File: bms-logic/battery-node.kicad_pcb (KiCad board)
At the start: 2 copper layers, 270.1 x 230.8 mm, 222 parts, among them J5 Connector, USB-TYPE-C-16P, Q1 PBSS4350T,215, Q10 PBSS4350T,215, Q11 PBSS4350T,215, Q12 PBSS4350T,215, Q13 PBSS4350T,215, Q14 PBSS4350T,215, Q15 PBSS4350T,215, Q16 PBSS4350T,215, Q17 PBSS4350T,215, Q18 PBSS4350T,215, Q19 PBSS4350T,215, Q2 BSS123, Q3 DMZ6012E, Q4 DMZ6012E, Q5 PBSS4350T,215, Q6 PBSS4350T,215, Q7 PBSS4350T,215, Q8 PBSS4350T,215, Q9 PBSS4350T,215, U1 ESP32-H2-MINI-1-H2S, U10 TCAN334D, U2 BQ76972PFBR, U3 2SC2383_C41375137, U4 XC6206P332MR, U5 MP9485GN-Z, U6 MIE1W0505BGLVH-3R-Z, U7 ISO7041FDBQ, U8 ADUM3160, U9 LTV-217-B-G

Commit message: started afe layout
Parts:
- removed the C21 at (34.3, 53.0)
- removed the C3 at (85.4, 25.2)
- removed the C4 at (85.4, 27.1)
- removed the C5 at (85.4, 28.9)
- removed the C50 at (110.6, -16.8)
- removed the C51 at (97.0, -16.8)
- removed the C52 at (102.2, -28.7)
- removed the C53 at (83.4, -5.49)
- removed the C6 at (85.4, 30.8)
- removed D6: SMCJ64CA, PCM_JLCPCB:D_SMC
- added C17: 220nF, PCM_JLCPCB:C_0805, B.Cu at (63.5, 25.7)
- added C36: 220nF, PCM_JLCPCB:C_0805, B.Cu at (63.5, 29.7)
- added C37: 220nF, PCM_JLCPCB:C_0805, B.Cu at (63.5, 33.6)
- added C38: 220nF, PCM_JLCPCB:C_0805, B.Cu at (63.5, 37.6)
- added C39: 220nF, PCM_JLCPCB:C_0805, B.Cu at (63.5, 41.6)
- added D16: BZT52C75, PCM_JLCPCB:D_SOD-123, F.Cu at (59.4, -99.3)
- added D17: BZT52C75, PCM_JLCPCB:D_SOD-123, F.Cu at (59.4, -95.9)
- C1, C2, C40, C41, C42, C43, C44, C45, C46, C47, C48, C49, Q1, Q10, Q11, Q12, Q13, Q14, Q15, Q16, Q17, Q18, Q19, Q6, Q7, Q8, Q9, R13, R14, R49, R50, R52, R53, R55, R56, R58, R59, R61, R62, R64, R65, R67, R68, R70, R71, R73, R74, R76, R77, R79, R80, R82, R83, R85, R86, R88, R89: moved to B.Cu
- CN1, CN2, CN3, CN4: value ~ -> A2001WR-S-2P
- D14: value ~ -> BAT20JFILM
- LED1: value ~ -> MHT136UBCT
- U2: renamed from U11; value ~ -> A2001WR-S-12PD01
- U3: renamed from U12; value ~ -> A2001WR-S-08PD01
- U4: renamed from U2; moved to B.Cu
- moved CN4 297.9 mm to (354.8, -26.8)
- moved CN3 294.0 mm to (343.9, -26.8)
- moved C50 280.1 mm to (318.2, -20.4)
- moved CN1 280.1 mm to (322.2, -26.8)
- moved C52 272.5 mm to (318.2, -16.7)
- moved CN2 272.1 mm to (333.1, -26.8)
- moved C53 266.1 mm to (318.2, -14.8)
- moved C51 261.4 mm to (318.2, -18.5)
- moved REF** 260.6 mm to (69.8, -10.2)
- moved JP3 178.3 mm to (219.2, -74.2)
- moved JP4 178.3 mm to (219.2, -70.6)
- moved Q4 175.8 mm to (214.3, -68.8)
- moved Q3 175.8 mm to (214.3, -73.5)
- moved D10 170.9 mm to (208.8, -64.2)
- moved D7 170.9 mm to (208.8, -74.3)
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- renumbered C14 to C10, C15 to C11, C16 to C12, C17 to C13, C18 to C14, C19 to C15, C20 to C16, C22 to C18, C23 to C19, C24 to C20, C25 to C21, C26 to C22, C27 to C23, C28 to C24, C29 to C25, C30 to C26, C31 to C27, C32 to C28, C33 to C29, C7 to C3, C34 to C30, C35 to C31, C36 to C32, C37 to C33, C38 to C34, C39 to C35, C8 to C4, C9 to C5, C6 to C50, C54 to C51, C55 to C52, C56 to C53, C10 to C6, C11 to C7, C12 to C8, C13 to C9, J5 to J3, U8 to U10, U9 to U11, U10 to U12, U3 to U5, U4 to U6, U5 to U7, U6 to U8, U7 to U9
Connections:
- C40 pad 1: /AFE/VC3 -> /AFE/VC7
- C40 pad 2: /AFE/VC2 -> /AFE/VC6
- C41 pad 1: /AFE/VC4 -> /AFE/VC8
- C41 pad 2: /AFE/VC3 -> /AFE/VC7
- C42 pad 1: /AFE/VC5 -> /AFE/VC9
- C42 pad 2: /AFE/VC4 -> /AFE/VC8
- C43 pad 1: /AFE/VC6 -> /AFE/VC10
- C43 pad 2: /AFE/VC5 -> /AFE/VC9
- C44 pad 1: /AFE/VC7 -> /AFE/VC11
- C44 pad 2: /AFE/VC6 -> /AFE/VC10
- C45 pad 1: /AFE/VC8 -> /AFE/VC12
- C45 pad 2: /AFE/VC7 -> /AFE/VC11
- C46 pad 1: /AFE/VC9 -> /AFE/VC13
- C46 pad 2: /AFE/VC8 -> /AFE/VC12
- C47 pad 1: /AFE/VC10 -> /AFE/VC14
- C47 pad 2: /AFE/VC9 -> /AFE/VC13
- C48 pad 1: /AFE/VC11 -> /AFE/VC15
- C48 pad 2: /AFE/VC10 -> /AFE/VC14
- C49 pad 1: /AFE/VC12 -> /AFE/VC16
- C49 pad 2: /AFE/VC11 -> /AFE/VC15
- R1 pad 2: +3V3 -> 3V3
- R2 pad 2: +3V3 -> 3V3
- R4 pad 2: +3V3 -> 3V3
- TP10 pad 1: +3V3 -> 3V3
- U1 pad 3: +3V3 -> 3V3
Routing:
- net Net-(Q7-C): track 0.00 -> 3.83 mm, vias 0 -> 1
- net Net-(Q19-C): track 0.00 -> 3.83 mm, vias 0 -> 1
- net Net-(Q18-C): track 0.00 -> 3.83 mm, vias 0 -> 1
- net Net-(Q17-C): track 0.00 -> 3.83 mm, vias 0 -> 1
- net Net-(Q16-C): track 0.00 -> 3.83 mm, vias 0 -> 1
- net Net-(Q15-C): track 0.00 -> 3.83 mm, vias 0 -> 1
- net Net-(Q14-C): track 0.00 -> 3.83 mm, vias 0 -> 1
- net Net-(Q13-C): track 0.00 -> 3.83 mm, vias 0 -> 1
- net Net-(Q12-C): track 0.00 -> 3.83 mm, vias 0 -> 1
- net Net-(Q6-C): track 0.00 -> 3.83 mm, vias 0 -> 1
- net Net-(Q5-C): track 0.00 -> 3.83 mm, vias 0 -> 1
- net Net-(Q1-C): track 0.00 -> 3.83 mm, vias 0 -> 1
- net Net-(Q9-C): track 0.00 -> 3.83 mm, vias 0 -> 1
- net Net-(Q8-C): track 0.00 -> 3.83 mm, vias 0 -> 1
- net Net-(Q11-C): track 0.00 -> 3.83 mm, vias 0 -> 1
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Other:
- copper layers 2 -> 4

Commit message: power supply layout
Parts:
- added TP23: IO25, TestPoint:TestPoint_Pad_D1.0mm, F.Cu at (216.9, 43.9)
- C18, C20, C22, C24, C32, C33, C34, C35, D13, D2, R12, R34, R35, U10: moved to B.Cu
- moved C20 193.5 mm to (76.7, 46.7), turned to 0 degrees
- moved C24 192.8 mm to (76.7, 56.4)
- moved U7 184.7 mm to (76.4, 49.5), turned to -90 degrees
- moved C19 182.3 mm to (76.7, 44.4), turned to 0 degrees
- moved L1 181.2 mm to (76.9, 55.9), turned to -90 degrees
- moved D13 177.8 mm to (74.9, 50.3)
- moved TP15 177.6 mm to (76.7, 59.2)
- moved R33 171.9 mm to (77.8, 35.2)
- moved R35 168.6 mm to (78.2, 48.2), turned to 180 degrees
- moved C18 167.7 mm to (76.7, 44.4), turned to 0 degrees
- moved R34 165.9 mm to (78.7, 49.8)
- moved JP5 165.1 mm to (75.8, 35.1)
- moved C23 164.7 mm to (74.1, 57.1)
- moved C21 162.6 mm to (74.1, 54.3), turned to -90 degrees
- moved C22 162.2 mm to (78.0, 51.3), turned to 0 degrees
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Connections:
- net /ISOLATED_COMMS/CAN_SHUTDOWN renamed /CAN_SHUTDOWN
- net /ISOLATED_COMMS/CAN_SLEEP renamed /CAN_SLEEP
- net /ISOLATED_COMMS/EN_ISO_PWR renamed /EN_ISO_PWR
- net /ISOLATED_COMMS/USB_N renamed /USB_D-
- net /ISOLATED_COMMS/USB_P renamed /USB_D+
- net /ISOLATED_COMMS/USB_nINT renamed /USB_nINT
- C22 pad 1: GND -> Net-(U7-FB)
- R34 pad 2: GND -> Net-(U7-FB)
- R35 pad 1: GND -> Net-(U7-FB)
- U1 pad 24: unconnected-(U1-IO22-Pad24) -> Net-(U1-IO22)
- U7 pad 1: GND -> Net-(U7-FB)
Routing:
- net (no net): track 0.00 -> 34.7 mm
- net GND: track 2.30 -> 18.9 mm, vias 2 -> 8
- net 5V0_SW: track 0.00 -> 12.8 mm, vias 0 -> 6
- net Net-(U7-BST): track 0.00 -> 10.4 mm, vias 0 -> 2
- net TOP_CELL: track 0.00 -> 8.87 mm, vias 0 -> 2
- net Net-(U7-FB): track 0.00 -> 5.54 mm, vias 0 -> 1
- net /AFE/VC0: track 0.00 -> 5.08 mm, vias 0 -> 1
- net Net-(D14-A): track 0.00 -> 4.23 mm
- net Net-(Q19-B): track 0.00 -> 4.17 mm
- net /EN_ISO_PWR: track 0.00 -> 4.14 mm
- net /AFE/Cell16: track 0.00 -> 3.58 mm, vias 0 -> 1
- net /AFE/VC16: track 0.00 -> 2.04 mm
- net Net-(U7-SW): track 0.00 -> 2.01 mm, vias 0 -> 1
- net GNDISO: track 0.00 -> 1.99 mm, vias 0 -> 2
- net 3V3: track 0.00 -> 1.68 mm, vias 0 -> 1
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- added copper zone on B.Cu, net /AFE/VC15
- added copper zone on In2.Cu, net 3V3
- added copper zone on B.Cu, net 5V0_ISO_SW
- added copper zone on B.Cu, net 5V0_SW
- added copper zone on F.Cu, net 5V0_SW
- added copper zone on B.Cu, net GND
- added copper zone on F.Cu, net GND
- added copper zone on In1.Cu, net GND
- added copper zone on F.Cu, net Net-(U7-SW)
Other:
- board size 270.1 x 230.8 mm -> 40.1 x 65.3 mm

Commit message: isolated comms
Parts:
- removed C50, C51, C52, C53: 470pF, PCM_JLCPCB:C_0402
- removed CN2, CN3, CN4: A2001WR-S-2P, JLCImport:A2001WR-S-2P
- removed JP6: SolderJumper_2_Open, Jumper:SolderJumper-2_P1.3mm_Open_RoundedPad1.0x1.5mm
- removed REF**: Untitled, ct_lib:Untitled
- removed TP1, TP10, TP11, TP2, TP23, TP3, TP4, TP5, TP6: IO25, TestPoint:TestPoint_Pad_D1.0mm
- removed TP16, TP17, TP18, TP19: IO8, TestPoint:TestPoint_Pad_D1.0mm
- removed TP7, TP8, TP9: IO9, TestPoint:TestPoint_Pad_D1.0mm
- removed U3: A2001WR-S-08PD01, JLCImport:A2001WR-S-08PD01
- added C54: 100nF, PCM_JLCPCB:C_0402, F.Cu at (79.3, 61.1)
- added C55: 100nF, PCM_JLCPCB:C_0402, F.Cu at (77.0, 72.9)
- added CN5: S4B-ZR-SM4A-TF_LF_SN, Connector_JST:JST_ZH_S4B-ZR-SM4A-TF_1x04-1MP_P1.50mm_Horizontal, F.Cu at (68.1, 79.5)
- C13, C27, C28, C30, C31, D11, R38, R39, R42, R43, R44, U11, U12: moved to B.Cu
- CN1: value A2001WR-S-2P -> S12B-ZR-SM4A-TF; footprint JLCImport:A2001WR-S-2P -> Connector_JST:JST_ZH_S12B-ZR-SM4A-TF_1x12-1MP_P1.50mm_Horizontal
- U2: value A2001WR-S-12PD01 -> S8B-ZR-SM4A-TF_LF_SN; footprint JLCImport:A2001WR-S-12PD01 -> Connector_JST:JST_ZH_S8B-ZR-SM4A-TF_1x08-1MP_P1.50mm_Horizontal
- U4: moved to F.Cu
- moved CN1 294.1 mm to (45.3, 72.3), turned to -90 degrees
- moved R1 135.3 mm to (116.5, 40.6)
- moved R2 135.3 mm to (118.3, 40.6)
- moved R4 123.6 mm to (119.1, 42.9)
- moved LED1 121.6 mm to (116.6, 43.7)
- moved R3 116.4 mm to (120.2, 40.6)
- moved C28 112.0 mm to (68.1, 61.0), turned to -90 degrees
- moved R40 109.8 mm to (68.0, 71.3), turned to -90 degrees
- moved R38 109.6 mm to (72.1, 59.4), turned to 0 degrees
- moved C27 109.6 mm to (70.1, 59.4), turned to 180 degrees
- moved R39 109.4 mm to (74.2, 59.4), turned to 180 degrees
- moved U11 109.0 mm to (81.3, 67.3)
- moved R42 107.0 mm to (74.0, 72.7), turned to 180 degrees
- moved U12 106.7 mm to (71.1, 79.0), turned to -90 degrees
- moved C30 106.3 mm to (69.3, 73.2), turned to -90 degrees
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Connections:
- C31 pad 1: GND -> GNDISO
- CN1 pad 2: /AFE/TEMP_CELLS_1 -> /AFE/Cell0
- CN1 pad 3: GND -> /AFE/Cell2
- CN1 pad 4: GND -> /AFE/Cell4
- U2 pad 1: unconnected-(U2-Pad1) -> /AFE/Cell1
- U2 pad 2: /AFE/Cell0 -> /AFE/Cell3
- U2 pad 3: /AFE/Cell2 -> /AFE/Cell5
- U2 pad 4: /AFE/Cell4 -> /AFE/Cell7
- U2 pad 5: /AFE/Cell6 -> /AFE/Cell9
- U2 pad 6: /AFE/Cell8 -> /AFE/Cell11
- U2 pad 7: /AFE/Cell10 -> /AFE/Cell13
- U2 pad 8: /AFE/Cell12 -> /AFE/Cell15
- U9 pad 13: Net-(JP6-A) -> unconnected-(U9-OUTB-Pad13)
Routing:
- net GNDISO: track 1.99 -> 68.5 mm, vias 2 -> 15
- net (no net): track 34.7 -> 0.00 mm
- net Net-(U12-CANH): track 0.00 -> 18.9 mm, vias 0 -> 1
- net Net-(U12-STB): track 0.00 -> 17.5 mm, vias 0 -> 3
- net Net-(JP7-A): track 0.00 -> 15.3 mm, vias 0 -> 1
- net Net-(U12-TXD): track 0.00 -> 13.8 mm, vias 0 -> 1
- net /ISOLATED_COMMS/USB_ISO_N: track 0.00 -> 10.2 mm, vias 0 -> 1
- net VBUS_ISO: track 0.00 -> 9.80 mm, vias 0 -> 4
- net Net-(U12-RXD): track 0.00 -> 9.65 mm, vias 0 -> 1
- net /ISOLATED_COMMS/USB_ISO_P: track 0.00 -> 8.61 mm, vias 0 -> 1
- net Net-(U10-SPD): track 0.00 -> 7.04 mm, vias 0 -> 1
- net 5V0_ISO_SW: track 0.00 -> 6.77 mm, vias 3 -> 6
- net GND: track 18.9 -> 23.8 mm, vias 8 -> 18
- net Net-(D11-K): track 0.00 -> 3.80 mm, vias 0 -> 1
- net Net-(U10-VDD2): track 0.00 -> 3.30 mm
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- added copper zone on F.Cu, net 3V3
- added copper zone on F.Cu, net 5V0_ISO_SW
- added copper zone on In2.Cu, net 5V0_ISO_SW
- added copper zone on In2.Cu, net 5V0_SW
- added copper zone on B.Cu, net GNDISO
- added copper zone on F.Cu, net GNDISO
- added copper zone on In1.Cu, net GNDISO
- added copper zone on In2.Cu, net VBUS_ISO
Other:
- board size 40.1 x 65.3 mm -> 45.2 x 65.3 mm
- board text added: "Add mounting holes for a custom heatsink over resistors? or just glue aluminum to them Or do nothing! They're rated for it anyways"
- board text added: "COMMS connection here?"
- board text added: "Cell connectors here"
- board text added: "Make mezzanine connector on bottom side 1.27 pitch ribbon on top side best of both worlds"

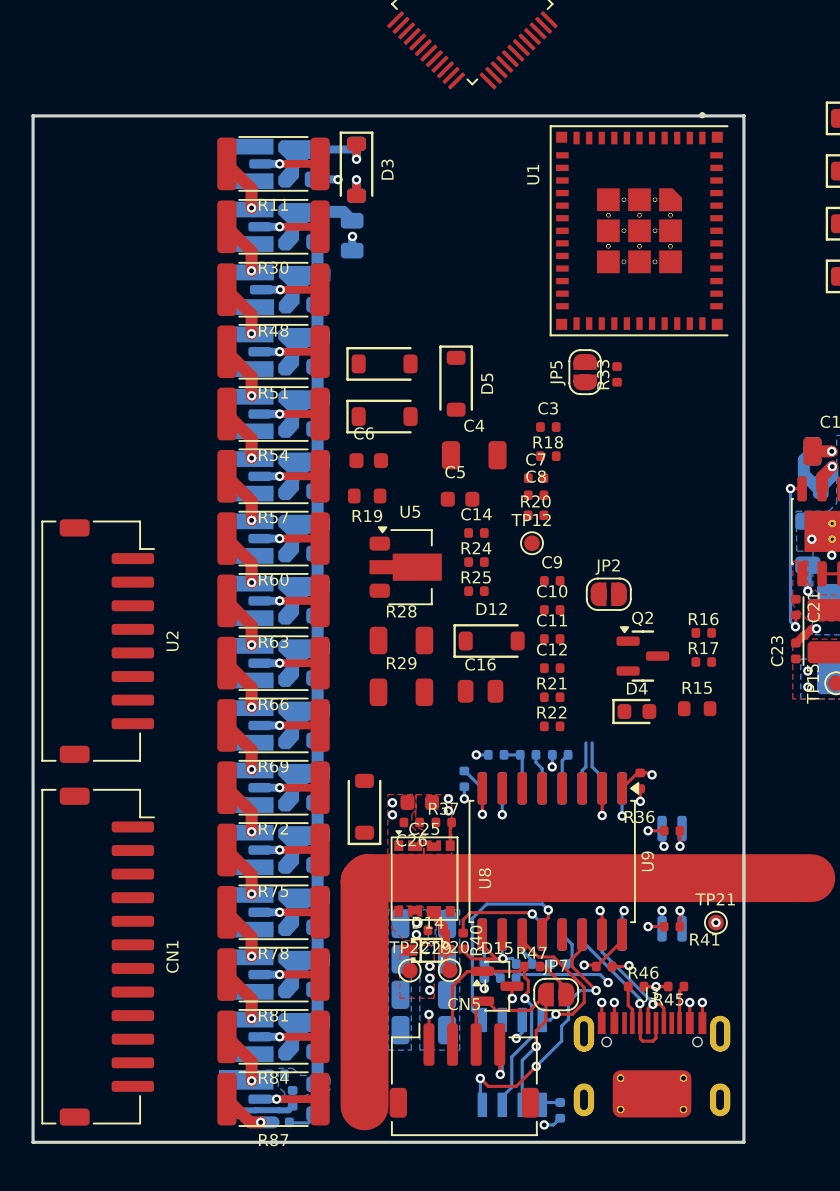
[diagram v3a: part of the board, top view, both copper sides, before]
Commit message: trying to flip resistor directions (fail)
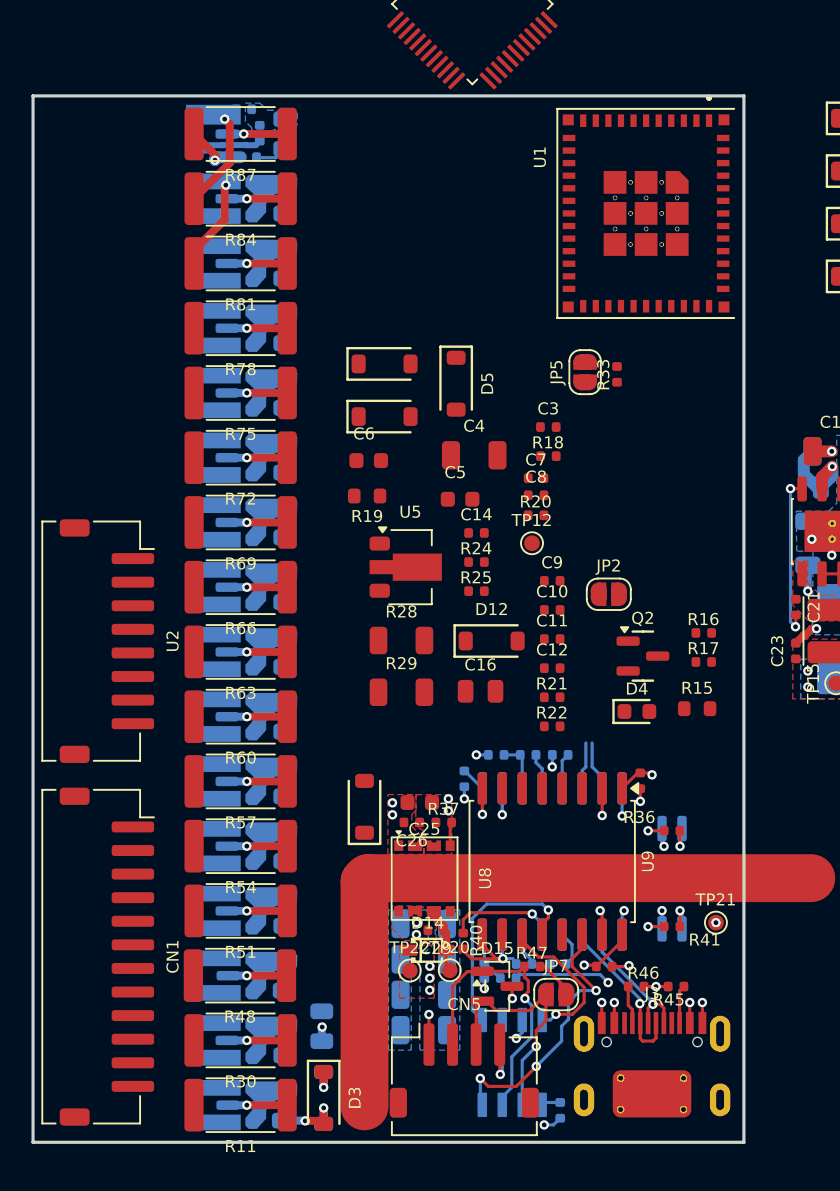
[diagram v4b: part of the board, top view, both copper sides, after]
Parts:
- moved R12 61.4 mm to (54.4, 21.4)
- moved C49 61.4 mm to (56.6, 19.9)
- moved Q19 61.4 mm to (52.0, 19.9)
- moved R87 61.4 mm to (53.8, 19.9)
- moved R88 61.4 mm to (55.1, 19.9)
- moved R89 61.4 mm to (54.0, 18.4)
- moved C2 59.9 mm to (56.6, 81.7)
- moved Q1 59.9 mm to (52.1, 81.7)
- moved R11 59.9 mm to (53.8, 81.7)
- moved R13 59.9 mm to (54.0, 82.9)
- moved R14 59.9 mm to (54.0, 80.6)
- moved D2 59.1 mm to (59.1, 81.3)
- moved D3 59.1 mm to (59.1, 81.3)
- moved C48 53.3 mm to (56.6, 24.1)
- moved Q18 53.3 mm to (52.0, 24.1)
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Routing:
- net /AFE/Cell8: track 3.45 -> 0.00 mm, vias 1 -> 0
- net /AFE/Cell7: track 3.45 -> 0.00 mm, vias 1 -> 0
- net /AFE/Cell6: track 3.45 -> 0.00 mm, vias 1 -> 0
- net /AFE/Cell5: track 3.45 -> 0.00 mm, vias 1 -> 0
- net /AFE/Cell4: track 3.45 -> 0.00 mm, vias 1 -> 0
- net /AFE/Cell13: track 3.45 -> 0.00 mm, vias 1 -> 0
- net /AFE/Cell12: track 3.45 -> 0.00 mm, vias 1 -> 0
- net /AFE/Cell9: track 3.45 -> 0.00 mm, vias 1 -> 0
- net /AFE/Cell11: track 3.45 -> 0.00 mm, vias 1 -> 0
- net /AFE/Cell10: track 3.45 -> 0.00 mm, vias 1 -> 0
- net /AFE/Cell3: track 3.45 -> 0.00 mm, vias 1 -> 0
- net /AFE/Cell2: track 3.45 -> 0.00 mm, vias 1 -> 0
- net /AFE/Cell1: track 3.45 -> 0.00 mm, vias 1 -> 0
- net /AFE/VC0: track 5.08 -> 1.96 mm
- net /AFE/Cell15: track 3.45 -> 6.14 mm
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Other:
- board size 45.2 x 65.3 mm -> 45.2 x 66.5 mm
- board text removed: "Cell connectors here"

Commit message: diagonal
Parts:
- added C50: 470pF, PCM_JLCPCB:C_0402, F.Cu at (34.8, 30.0)
- added C51: 470pF, PCM_JLCPCB:C_0402, F.Cu at (37.0, 30.0)
- added C56: 470pF, PCM_JLCPCB:C_0402, F.Cu at (34.8, 31.9)
- added C57: 470pF, PCM_JLCPCB:C_0402, F.Cu at (37.0, 31.9)
- added CN2: S4B-ZR-SM4A-TF_LF_SN, JLCImport:JST_ZH_S4B-ZR-SM4A-TF_1x04-1MP_P1.50mm_Horizontal, F.Cu at (45.3, 25.2)
- added CN3: S4B-ZR-SM4A-TF_LF_SN, JLCImport:JST_ZH_S4B-ZR-SM4A-TF_1x04-1MP_P1.50mm_Horizontal, F.Cu at (45.3, 36.3)
- added TP1: IO25, TestPoint:TestPoint_Pad_D1.0mm, F.Cu at (6.08, 1.02)
- added TP10: IO25, TestPoint:TestPoint_Pad_D1.0mm, F.Cu at (15.2, 1.02)
- added TP11: IO25, TestPoint:TestPoint_Pad_D1.0mm, F.Cu at (15.2, 4.08)
- added TP16: IO8, TestPoint:TestPoint_Pad_D1.0mm, F.Cu at (1.02, 1.02)
- added TP17: IO8, TestPoint:TestPoint_Pad_D1.0mm, F.Cu at (1.02, 4.08)
- added TP18: IO8, TestPoint:TestPoint_Pad_D1.0mm, F.Cu at (1.02, 7.12)
- added TP19: IO8, TestPoint:TestPoint_Pad_D1.0mm, F.Cu at (1.02, 10.2)
- added TP2: IO25, TestPoint:TestPoint_Pad_D1.0mm, F.Cu at (6.08, 4.08)
- added TP23: IO25, TestPoint:TestPoint_Pad_D1.0mm, F.Cu at (15.2, 7.12)
- added TP3: IO25, TestPoint:TestPoint_Pad_D1.0mm, F.Cu at (6.08, 7.12)
- added TP4: IO25, TestPoint:TestPoint_Pad_D1.0mm, F.Cu at (9.12, 1.02)
- added TP5: IO25, TestPoint:TestPoint_Pad_D1.0mm, F.Cu at (9.12, 4.08)
- added TP6: IO25, TestPoint:TestPoint_Pad_D1.0mm, F.Cu at (9.12, 7.12)
- added TP7: IO9, TestPoint:TestPoint_Pad_D1.0mm, F.Cu at (12.2, 1.02)
- added TP8: IO9, TestPoint:TestPoint_Pad_D1.0mm, F.Cu at (12.2, 4.08)
- added TP9: IO9, TestPoint:TestPoint_Pad_D1.0mm, F.Cu at (12.2, 7.12)
- C1: moved to F.Cu
- C4, C5, C6, D1, D16, D17, D5, R19: moved to B.Cu
- CN1: footprint Connector_JST:JST_ZH_S12B-ZR-SM4A-TF_1x12-1MP_P1.50mm_Horizontal -> JLCImport:JST_ZH_S12B-ZR-SM4A-TF_1x12-1MP_P1.50mm_Horizontal
- CN5: footprint Connector_JST:JST_ZH_S4B-ZR-SM4A-TF_1x04-1MP_P1.50mm_Horizontal -> JLCImport:JST_ZH_S4B-ZR-SM4A-TF_1x04-1MP_P1.50mm_Horizontal
- U2: footprint Connector_JST:JST_ZH_S8B-ZR-SM4A-TF_1x08-1MP_P1.50mm_Horizontal -> JLCImport:JST_ZH_S8B-ZR-SM4A-TF_1x08-1MP_P1.50mm_Horizontal
- moved D2 67.3 mm to (66.4, 14.4)
- moved D3 67.3 mm to (66.4, 14.4)
- moved C1 67.3 mm to (66.3, 9.84)
- moved Q2 48.6 mm to (128.0, 53.0)
- moved R16 48.6 mm to (131.9, 51.6)
- moved R17 48.6 mm to (131.9, 53.4)
- moved D4 48.6 mm to (127.6, 56.6)
- moved JP2 48.6 mm to (125.8, 49.1)
- moved R15 48.6 mm to (131.4, 56.4)
- moved C10 43.4 mm to (110.4, 73.3)
- moved C11 43.4 mm to (110.4, 75.2)
- moved C12 43.4 mm to (110.4, 77.0)
- moved C7 43.4 mm to (109.4, 64.9)
- moved C8 43.4 mm to (109.4, 66.0)
- moved C9 43.4 mm to (110.4, 71.5)
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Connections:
- CN1 pad 1: GND -> unconnected-(CN1-Pad1)
- CN1 pad 10: /AFE/Cell16 -> /AFE/Cell2
- CN1 pad 11: TOP_CELL -> /AFE/Cell0
- CN1 pad 12: unconnected-(CN1-Pad12) -> GND
- CN1 pad 2: /AFE/Cell0 -> TOP_CELL
- CN1 pad 3: /AFE/Cell2 -> /AFE/Cell16
- CN1 pad 4: /AFE/Cell4 -> /AFE/Cell14
- CN1 pad 5: /AFE/Cell6 -> /AFE/Cell12
- CN1 pad 6: /AFE/Cell8 -> /AFE/Cell10
- CN1 pad 7: /AFE/Cell10 -> /AFE/Cell8
- CN1 pad 8: /AFE/Cell12 -> /AFE/Cell6
- CN1 pad 9: /AFE/Cell14 -> /AFE/Cell4
- U2 pad 1: /AFE/Cell1 -> /AFE/Cell15
- U2 pad 2: /AFE/Cell3 -> /AFE/Cell13
- U2 pad 3: /AFE/Cell5 -> /AFE/Cell11
- U2 pad 4: /AFE/Cell7 -> /AFE/Cell9
- U2 pad 5: /AFE/Cell9 -> /AFE/Cell7
- U2 pad 6: /AFE/Cell11 -> /AFE/Cell5
- U2 pad 7: /AFE/Cell13 -> /AFE/Cell3
- U2 pad 8: /AFE/Cell15 -> /AFE/Cell1
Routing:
- net /AFE/Cell16: track 3.98 -> 56.0 mm, vias 1 -> 2
- net /AFE/Cell14: track 5.82 -> 49.3 mm, vias 1 -> 2
- net /AFE/Cell12: track 0.00 -> 41.7 mm, vias 0 -> 2
- net /AFE/VC0: track 1.96 -> 40.8 mm, vias 1 -> 2
- net /AFE/Cell10: track 0.00 -> 35.0 mm, vias 0 -> 2
- net /AFE/Cell1: track 0.00 -> 31.0 mm, vias 0 -> 2
- net /AFE/VC16: track 2.04 -> 33.0 mm, vias 0 -> 1
- net /AFE/VC2: track 0.00 -> 30.2 mm, vias 0 -> 1
- net /AFE/VC15: track 0.00 -> 30.0 mm, vias 0 -> 1
- net /AFE/VC1: track 0.00 -> 29.9 mm, vias 0 -> 1
- net /AFE/Cell8: track 0.00 -> 28.5 mm, vias 0 -> 2
- net /AFE/Cell15: track 6.14 -> 32.1 mm, vias 1 -> 2
- net /AFE/VC3: track 0.00 -> 25.9 mm, vias 0 -> 2
- net /AFE/VC4: track 0.00 -> 25.8 mm, vias 0 -> 1
- net /AFE/VC14: track 0.00 -> 24.8 mm, vias 0 -> 1
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- added copper zone on F.Cu, net TOP_CELL
- added copper zone on In2.Cu, net TOP_CELL
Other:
- board size 45.2 x 66.5 mm -> 44.2 x 66.4 mm
